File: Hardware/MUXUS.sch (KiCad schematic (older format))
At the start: 3 parts

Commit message: Checkpoint
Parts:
- added C? (x18): 100nF, symbol Device:C_Small
- added C?: 4.7uF, symbol Device:C_Small
- added R?: 12K, symbol Device:R
- added R? (x3): 4K7, symbol Device:R
- added R? (x4): 200K, symbol Device:R
- added R?: 56K, symbol Device:R
- added U?: USB7002_KDX, QFN40P1200X1200X90-101N, symbol USB7002_KDX:USB7002_KDX
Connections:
- net +3V3: now reaches U?.2 (VDD/VDDA)
- net +3V3: now also C?.1, C?.1, C?.2, C?.2, C?.2, C?.2, C?.2, C?.2, C?.2, C?.2, R?.2, U?.26 (VDD33), U?.44 (VDD33), U?.53 (VDD33), U?.62 (VDD33), U?.67 (VDD33), U?.79 (VDD33), U?.86 (VDD33), U?.99 (VDD33)
- net GND: now reaches U?.3 (VSS/VSSA)
- net GND: now also C?.1, C?.1, C?.1, C?.1, C?.1, C?.1, C?.1, C?.1, C?.2, C?.2, C?.2, C?.2, C?.2, C?.2, C?.2, C?.2, C?.2, C?.2, C?.2, R?.1, R?.1, R?.1, R?.1, R?.1, R?.2, R?.2, U?.101 (VSS), U?.24 (TESTEN), U?.96 (ATEST)
- net NRST: now reaches U?.4 (PA0/PA1/PA2/NRST)
- net NRST: now also U?.1 (RESET_N)
- net SLV_I2C_CLK: now reaches U?.5 (PA8/PA11[PA9]/PB0/PB1)
- net SLV_I2C_CLK: now also U?.75 (PF26)
- net SLV_I2C_DATA: now reaches U?.6 (PA12[PA10])
- net SLV_I2C_DATA: now also U?.76 (PF27)
- net SYS_SWDIO: now reaches U?.7 (PA13)
- net SYS_SWCLK: now reaches U?.8 (PB5/PB6/PA14-BOOT0/PA15)
- new net: R?.2, U?.100 (RBIAS)
- new net: R?.2, U?.21 (CFG_STRAP1)
- new net: R?.2, U?.22 (CFG_STRAP2)
- new net: R?.1, U?.63 (TEST1)
- new net: R?.1, U?.64 (TEST2)
- new net: R?.1, U?.65 (TEST3)
- new net: R?.2, U?.69 (PF20/CFG_NON_REM)
- new net: R?.2, U?.70 (PF22/CFG_BC_EN)
- new net: R?.1, U?.87 (CC1_UP)
- new net +1V2: C?.1, C?.1, C?.1, C?.1, C?.1, C?.1, C?.1, C?.1, C?.1, U?.18 (VDD12), U?.25 (VDD12), U?.33 (VDD12), U?.41 (VDD12), U?.55 (VDD12), U?.78 (VDD12), U?.83 (VDD12), U?.9 (VDD12), U?.93 (VDD12)
- new net MSTR_I2C_CLK: U?.61 (PF18)
- new net MSTR_I2C_DATA: U?.66 (PF19)
- new net VBUS: R?.2
- no-connect marks 0 -> 7
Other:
- note added: "100nF SMD_0603 or smaller"
- moved on the sheet: U?

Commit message: Checkpoint
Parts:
- removed C? (x18): 100nF, symbol Device:C_Small
- removed C?: 4.7uF, symbol Device:C_Small
- removed R?: 12K, symbol Device:R
- removed R? (x3): 4K7, symbol Device:R
- removed R? (x4): 200K, symbol Device:R
- removed R?: 56K, symbol Device:R
- removed U? (x2): HD3SS3202IRSVT, QFN40P180X260X55-16N_HD3SS3202IRSVT, symbol HD3SS3202IRSVT:HD3SS3202IRSVT
- removed U?: STM32G030J6M6, SOIC127P600X175-8N, symbol STM32G030J6M6:STM32G030J6M6
- removed U?: USB7002_KDX, QFN40P1200X1200X90-101N, symbol USB7002_KDX:USB7002_KDX
- added C? (x11): 100nF, Capacitor_SMD:C_0805_2012Metric, symbol Device:C_Small
- added C? (x5): 4.7uF, symbol Device:C_Small
- added C?: 87pF, symbol Device:C
- added C? (x14): 100nF, Capacitor_SMD:C_0805_2012Metric, symbol Device:C
- added C?: 1uF, symbol Device:C_Small
- added C? (x2): 22uF, symbol Device:C
- added C?: 1uF, symbol Device:C
- added C? (x2): 14pF, symbol Device:C
- added C? (x3): 120uF, Capacitor_SMD:C_0805_2012Metric, symbol Device:C
- added D? (x4): AMBER, LED_SMD:LED_1206_3216Metric, symbol Device:LED
- added D? (x4): GREEN, LED_SMD:LED_1206_3216Metric, symbol Device:LED
- added D?: B540C-13-F, Diode_SMD:D_SMC, symbol Device:D_Schottky
- added D? (x4): LED, symbol Device:LED
- added F?: 500mA, Fuse:Fuse_1206_3216Metric, symbol Device:Polyfuse
- added J? (x3): USB_B, 67068-9000:67068-9000, symbol Connector:USB_B
- added J? (x3): USB_A, 67643-0910:67643-0910, symbol Connector:USB_A
- added J?: USB_C_Receptacle_USB2.0, DX07S016JA1R1500:DX07S016JA1R1500, symbol Connector:USB_C_Receptacle_USB2.0
- added J?: STDC14, symbol Connector_Generic:Conn_02x07_Odd_Even
- added L?: SRP6530A-6R8M, SRP6530A-6R8M:SRP6530A-6R8M, symbol Device:L
- added R? (x4): 10K, Resistor_SMD:R_1206_3216Metric, symbol Device:R
- added R?: 15.1K, symbol Device:R
- added R? (x7): 330R, symbol Device:R
- added R?: 31.6K, symbol Device:R_Small
- added R?: 10K, Resistor_SMD:R_1206_3216Metric, symbol Device:R_Small
- added R? (x3): 1K, symbol Device:R
- added R? (x12): 100R, symbol Device:R
- added R?: 12K, symbol Device:R
- added SW?: USER, symbol Switch:SW_Push
- added SW?: RESET, symbol Switch:SW_Push
- added U?: STM32G431K8T6, STM32G431K8T6:STM32G431K8T6, symbol STM32G431K8T6:STM32G431K8T6
- added U?: AOZ1212AI, Package_SO:SO-8_3.9x4.9mm_P1.27mm, symbol AOZ1212AI:AOZ1212AI
- added U?: TS3USBCA420RSVR, symbol TS3USBCA420RSVR:TS3USBCA420RSVR
- added U? (x6): USBLC6-2SC6, Package_TO_SOT_SMD:SOT-23-6, symbol Power_Protection:USBLC6-2SC6
- added U? (x3): AP2151W, Package_TO_SOT_SMD:SOT-23-5, symbol AP2151W:AP2151W
- added U?: USB2504A-JT, Package_QFP:LQFP-64_10x10mm_P0.5mm, symbol USB2504A-JT:USB2504A-JT
- added U?: USBLC6-4SC6, Package_TO_SOT_SMD:SOT-23-6, symbol Power_Protection:USBLC6-4SC6
- added Y?: ATS240C, symbol Device:Crystal
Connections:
- net +3V3: now also C?.1, C?.1, C?.1, C?.1, C?.1, C?.1, C?.2, C?.2, C?.2, C?.2, C?.2, C?.2, J?.3 (Pin_3), L?.2, R?.1, R?.1, R?.1, R?.1, R?.1, R?.1, R?.1, R?.1, R?.1, R?.2, R?.2, R?.2, R?.2, R?.2, R?.2, R?.2, R?.2, R?.2, R?.2, U?.1 (VCC), U?.1 (VDD), U?.1 (VDDA33), U?.12 (I2C_EN), U?.13 (VDDA33), U?.15 (VDDA/VREF+), U?.17 (VDD), U?.23 (PRTPWR_POL), U?.28 (VDD33), U?.51 (SELF_PWR), U?.61 (VDDA33PLL), U?.62 (ATEST/REG_EN), U?.7 (VDDA33)
- net GND: now also C?.1, C?.1, C?.1, C?.1, C?.1, C?.1, C?.1, C?.1, C?.1, C?.1, C?.1, C?.1, C?.1, C?.1, C?.1, C?.1, C?.1, C?.1, C?.1, C?.1, C?.1, C?.1, C?.1, C?.2, C?.2, C?.2, C?.2, C?.2, C?.2, C?.2, C?.2, C?.2, C?.2, C?.2, C?.2, C?.2, C?.2, C?.2, C?.2, D?.2 (A), J?.4 (GND), J?.4 (GND), J?.4 (GND), J?.4 (GND), J?.4 (GND), J?.4 (GND), J?.5 (Pin_5), J?.7 (Pin_7), J?.A1 (GND), J?.A12 (GND), J?.B1 (GND), J?.B12 (GND), R?.1, R?.1, R?.1, R?.1, R?.2, R?.2, R?.2, R?.2, R?.2, R?.2, SW?.2, SW?.2, U?.10 (VSS), U?.14 (VSSA), U?.16 (VSS), U?.16 (VSS), U?.2 (GND), U?.2 (GND), U?.2 (GND), U?.2 (GND), U?.2 (GND), U?.2 (GND), U?.2 (GND), U?.2 (GND), U?.2 (GND), U?.2 (GND), U?.29 (VSS), U?.3 (GND), U?.31 (TEST0), U?.32 (VSS), U?.36 (CFG_SEL0), U?.4 (OEn), U?.4 (VSS), U?.41 (VSS), U?.47 (CLKIN_EN), U?.48 (TEST1), U?.50 (CFG_SEL1), U?.53 (VSS), U?.55 (VSS), U?.59 (CFG_SEL2), U?.64 (VSS), U?.9 (GND)
- net NRST: now also C?.2, J?.12 (Pin_12), R?.1, SW?.1, U?.4 (PG10-NRST)
- net VBUS: now also C?.2, C?.2, C?.2, U?.5 (IN), U?.5 (IN), U?.5 (IN)
- new net: C?.2, D?.1 (K), L?.1, U?.1 (LX)
- new net: C?.1, U?.2 (BST)
- new net: R?.1, R?.2, U?.4 (FB)
- new net: R?.2, U?.5 (COMP)
- new net: C?.2, F?.1, U?.6 (EN), U?.7 (VIN)
- new net: C?.2, U?.8 (VBIAS)
- new net: C?.2, R?.1
- new net: C?.2, J?.S1 (SHIELD), R?.2
- new net: C?.1, J?.5 (Shield), R?.1 (x3)
- new net: C?.1, C?.1, J?.1 (VBUS), U?.1 (OUT), U?.5 (VBUS) (x3)
- new net: C?.2, J?.5 (Shield), R?.2 (x3)
- new net: C?.1, U?.57 (XTAL2), Y?.1
- new net: C?.2, U?.58 (XTAL1/CLKIN), Y?.2
- new net: D?.1 (K), U?.19 (AM4/LED_EN)
- new net: D?.1 (K), U?.20 (GR4/PRT_DIS1)
- new net: D?.1 (K), U?.21 (AM3)
- new net: D?.1 (K), U?.22 (GR3/PRT_DIS0)
- new net: D?.1 (K), U?.24 (AM2/MTT_EN)
- new net: D?.1 (K), U?.25 (GR2/NON_REM1)
- new net: D?.1 (K), U?.26 (AM1/GANG_EN)
- new net: D?.1 (K), U?.27 (GR1/NON_REM0)
- new net: C?.2, C?.2, C?.2, C?.2, U?.30 (VDD18), U?.42 (VDD18), U?.54 (VDD18), U?.60 (VDDA18PLL)
- new net: R?.1, U?.63 (RBIAS)
- new net: D?.2 (A), R?.1 (x8)
- new net: D?.2 (A), R?.2 (x4)
- new net BOOT0: R?.1, U?.31 (PB8-BOOT0)
- new net CC1: J?.A5 (CC1), U?.19 (PA9), U?.29 (PB6), U?.4 (I/O3)
- new net CC2: J?.B5 (CC2), U?.20 (PA10), U?.27 (PB4), U?.6 (I/O4)
- new net DFP1_D+: U?.22 (PA12), U?.6 (USBDP1)
- new net DFP1_D-: U?.21 (PA11), U?.5 (USBDN1)
- new net DFP2_CONN_D+: J?.3 (D+), U?.3 (I/O2)
- new net DFP2_CONN_D-: J?.2 (D-), U?.1 (I/O1)
- new net DFP2_D+: U?.4 (I/O2), U?.8 (USBDP2)
- new net DFP2_D-: U?.6 (I/O1), U?.9 (USBDN2)
- new net DFP2_EN: U?.4 (EN), U?.43 (PRTPWR2)
- new net DFP2_OCSn: U?.3 (~FLG), U?.44 (OCS2_N)
- new net DFP3_CONN_D+: J?.3 (D+), U?.3 (I/O2)
- new net DFP3_CONN_D-: J?.2 (D-), U?.1 (I/O1)
- new net DFP3_D+: U?.12 (USBDP3), U?.4 (I/O2)
- new net DFP3_D-: U?.11 (USBDN3), U?.6 (I/O1)
- new net DFP3_EN: U?.39 (PRTPWR3), U?.4 (EN)
- new net DFP3_OCSn: U?.3 (~FLG), U?.40 (OCS3_N)
- new net DFP4_CONN_D+: J?.3 (D+), U?.3 (I/O2)
- new net DFP4_CONN_D-: J?.2 (D-), U?.1 (I/O1)
- new net DFP4_D+: U?.14 (USBDP4), U?.4 (I/O2)
- new net DFP4_D-: U?.15 (USBDN4), U?.6 (I/O1)
- new net DFP4_EN: U?.37 (PRTPWR4), U?.4 (EN)
- new net DFP4_OCSn: U?.3 (~FLG), U?.38 (OCS4_N)
- new net HUB_RESET: R?.2, U?.13 (PB0), U?.49 (RESET_N)
- new net I2C1_SCL: U?.25 (PA15), U?.35 (SCL/SMBCLK), U?.5 (SEL1/SCL)
- new net I2C1_SDA: R?.2, U?.30 (PB7), U?.34 (SDA/SMBDATA), U?.6 (SEL0/SDA)
- new net I2C1_SMBA: R?.2, U?.28 (PB5)
- new net IFP_D+: U?.11 (SBU1), U?.2 (USBDP0)
- new net IFP_D-: U?.10 (SBU2), U?.3 (USBDN0)
- new net IFP_VBUS: R?.2, U?.12 (PA7), U?.52 (VBUS_DET)
- new net LPUART1_RX: J?.13 (Pin_13), U?.8 (PA3)
- new net LPUART1_TX: J?.14 (Pin_14), U?.7 (PA2)
- new net SWCLK: J?.6 (Pin_6), U?.24 (PA14)
- new net SWDIO: J?.4 (Pin_4), U?.23 (PA13)
- new net SWO: J?.8 (Pin_8), U?.26 (PB3)
- new net UFP1_D+: J?.A6 (D+), J?.B6 (D+), U?.3 (I/O2), U?.7 (LnBp)
- new net UFP1_D-: J?.A7 (D-), J?.B7 (D-), U?.1 (I/O1), U?.8 (LnBn)
- new net UFP1_VBUS: F?.2, J?.A4 (VBUS), J?.A9 (VBUS), J?.B4 (VBUS), J?.B9 (VBUS), U?.5 (VBUS)
- new net UFP2_CONN_D+: J?.3 (D+), U?.1 (I/O1)
- new net UFP2_CONN_D-: J?.2 (D-), U?.3 (I/O2)
- new net UFP2_D+: U?.2 (MIC_GND1/Ln1), U?.6 (I/O1)
- new net UFP2_D-: U?.3 (MIC_GND2/Ln2), U?.4 (I/O2)
- new net UFP2_VBUS: J?.1 (VBUS), U?.5 (VBUS), U?.9 (PA4)
- new net UFP3_CONN_D+: J?.3 (D+), U?.1 (I/O1)
- new net UFP3_CONN_D-: J?.2 (D-), U?.3 (I/O2)
- new net UFP3_D+: U?.14 (LnCp), U?.6 (I/O1)
- new net UFP3_D-: U?.13 (LnCn), U?.4 (I/O2)
- new net UFP3_VBUS: J?.1 (VBUS), U?.10 (PA5), U?.5 (VBUS)
- new net UFP4_CONN_D+: J?.3 (D+), U?.1 (I/O1)
- new net UFP4_CONN_D-: J?.2 (D-), U?.3 (I/O2)
- new net UFP4_D+: U?.16 (LnAp), U?.6 (I/O1)
- new net UFP4_D-: U?.15 (LnAn), U?.4 (I/O2)
- new net UFP4_VBUS: J?.1 (VBUS), U?.11 (PA6), U?.5 (VBUS)
- new net UI_BUTTON: C?.2, R?.1, SW?.1, U?.18 (PA8)
- new net UI_LED1: D?.1 (K), U?.2 (PF0-OSC_IN)
- new net UI_LED2: D?.1 (K), U?.3 (PF1-OSC_OUT)
- new net UI_LED3: D?.1 (K), U?.5 (PA0)
- new net UI_LED4: D?.1 (K), U?.6 (PA1)
- no-connect marks 7 -> 9
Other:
- note added: "create footprint"
- note removed: "100nF SMD_0603 or smaller"

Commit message: Checkpoint
Supposed finalization of first prototype
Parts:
- removed R?: 10K, Resistor_SMD:R_1206_3216Metric, symbol Device:R
- added R12, R13, R14: 10K, Resistor_SMD:R_1206_3216Metric, symbol Device:R
- added R16, R18, R20: 1K, Resistor_SMD:R_1206_3216Metric, symbol Device:R
- C1, C2: renamed from C?; value 14pF -> 15pF; footprint (none) -> Capacitor_SMD:C_0805_2012Metric
- C15, C28, C37: renamed from C?; footprint Capacitor_SMD:C_0805_2012Metric -> Capacitor_THT:C_Radial_D6.3mm_H11.0mm_P2.50mm
- C16, C31: renamed from C?; footprint (none) -> Capacitor_SMD:C_0805_2012Metric
- C25, C4, C5, C6, C7: renamed from C?; footprint (none) -> Capacitor_SMD:C_1206_3216Metric
- C30, C39: renamed from C?; footprint (none) -> Capacitor_SMD:C_1210_3225Metric
- C33: renamed from C?; value 87pF -> 100pF; footprint (none) -> Capacitor_SMD:C_0805_2012Metric
- D10, D11, D12, D9: renamed from D?; footprint (none) -> LED_THT:LED_D5.0mm
- J6: renamed from J?; footprint (none) -> FTSH-107-01-L-DV-K-A:FTSH-107-01-L-DV-K-A
- R1, R10, R11, R15, R17, R19, R24, R25, R28, R29, R30, R31, R33, R34, R5, R6, R7, R8, R9: renamed from R?; footprint (none) -> Resistor_SMD:R_0805_2012Metric
- R2, R21, R23, R35, R4: renamed from R?; footprint (none) -> Resistor_SMD:R_1206_3216Metric
- R32: renamed from R?; value 15.1K -> 15K; footprint (none) -> Resistor_SMD:R_1206_3216Metric
- SW1, SW2: renamed from SW?; footprint (none) -> Button_Switch_SMD:SW_Push_1P1T_NO_6x6mm_H9.5mm
- U6: renamed from U?; footprint (none) -> TS3USBCA420RSVR:TS3USBCA420RSVR
- Y1: renamed from Y?; footprint (none) -> ATS240C:ATS240C
- gave numbers to parts that had none: 60
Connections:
- net UFP1_VBUS is gone; now on net VBUS: F1.2, J1.A4 (VBUS), J1.A9 (VBUS), J1.B4 (VBUS), J1.B9 (VBUS), U1.5 (VBUS)
- net +3V3: now also C26.1, SW1.2
- net BOOT0: now also C26.2, R22.2, SW1.1; no longer R22.1
- net GND: now also R22.1, R16.2, R18.2, R20.2; no longer C26.1, R22.2, SW1.2
- net I2C1_SCL: now also R21.2
- net I2C1_SMBA: no longer R21.2
- net UFP2_VBUS: now also R12.2; no longer U7.9 (PA4)
- net UFP3_VBUS: now also R13.2; no longer U7.10 (PA5)
- net UFP4_VBUS: now also R14.2; no longer U7.11 (PA6)
- removed net UI_BUTTON: C26.2, SW1.1, U7.18 (PA8)
- new net: R13.1, R18.1, U7.10 (PA5)
- new net: R14.1, R16.1, U7.11 (PA6)
- new net: R12.1, R20.1, U7.9 (PA4)
- no-connect marks 9 -> 10
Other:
- moved on the sheet: C26, C27, R21, R22, R23, R27, SW1, SW2

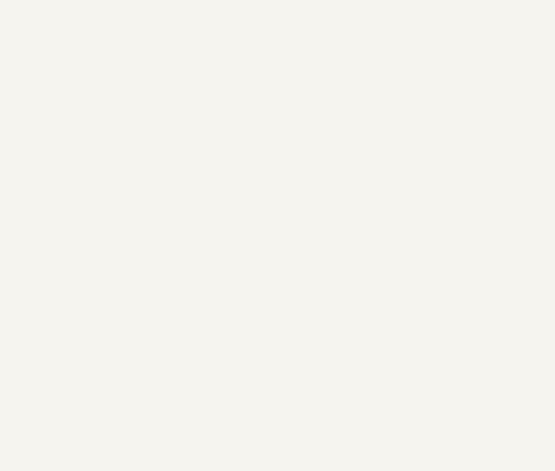
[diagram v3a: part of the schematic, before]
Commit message: Mounting holes
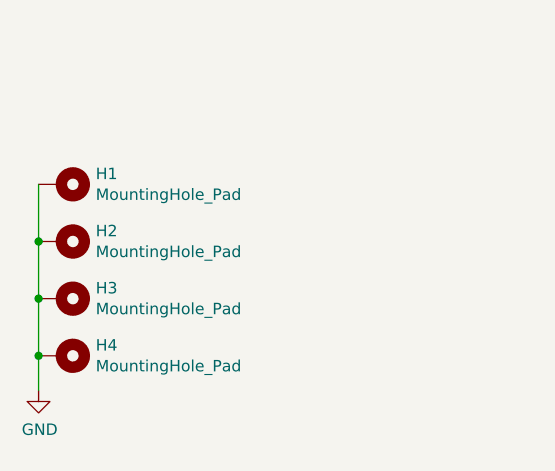
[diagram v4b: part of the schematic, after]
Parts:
- added H1, H2, H3, H4: MountingHole_Pad, MountingHole:MountingHole_3.2mm_M3_Pad_Via, symbol Mechanical:MountingHole_Pad
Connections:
- net GND: now also H1.1, H2.1, H3.1, H4.1
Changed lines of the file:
@@
 Wire Wire Line
 	9500 6700 9850 6700
+$Comp
+L Mechanical:MountingHole_Pad H1
+U 1 1 6152FF69
+P 950 10000
+F 0 "H1" V 904 10150 50  0000 L CNN
+F 1 "MountingHole_Pad" V 995 10150 50  0000 L CNN
+F 2 "MountingHole:MountingHole_3.2mm_M3_Pad_Via" H 950 10000 50  0001 C CNN
+F 3 "~" H 950 10000 50  0001 C CNN
+	1    950  10000
+	0    1    1    0
+$EndComp
+$Comp
+L Mechanical:MountingHole_Pad H3
+U 1 1 615352EC
+P 950 10500
+F 0 "H3" V 904 10650 50  0000 L CNN
+F 1 "MountingHole_Pad" V 995 10650 50  0000 L CNN
+F 2 "MountingHole:MountingHole_3.2mm_M3_Pad_Via" H 950 10500 50  0001 C CNN
+F 3 "~" H 950 10500 50  0001 C CNN
+	1    950  10500
+	0    1    1    0
+$EndComp
+$Comp
+L Mechanical:MountingHole_Pad H2
+U 1 1 61536034
+P 950 10250
+F 0 "H2" V 904 10400 50  0000 L CNN
+F 1 "MountingHole_Pad" V 995 10400 50  0000 L CNN
+F 2 "MountingHole:MountingHole_3.2mm_M3_Pad_Via" H 950 10250 50  0001 C CNN
+F 3 "~" H 950 10250 50  0001 C CNN
+	1    950  10250
+	0    1    1    0
+$EndComp
+$Comp
+L Mechanical:MountingHole_Pad H4
+U 1 1 61536512
+P 950 10750
+F 0 "H4" V 904 10900 50  0000 L CNN
+F 1 "MountingHole_Pad" V 995 10900 50  0000 L CNN
+F 2 "MountingHole:MountingHole_3.2mm_M3_Pad_Via" H 950 10750 50  0001 C CNN
+F 3 "~" H 950 10750 50  0001 C CNN
+	1    950  10750
+	0    1    1    0
+$EndComp
+Wire Wire Line
+	850  10000 850  10250
+Connection ~ 850  10250
+Wire Wire Line
+	850  10250 850  10500
+Connection ~ 850  10500
+Wire Wire Line
+	850  10500 850  10750
+Wire Wire Line
+	850  10750 850  10900
+Connection ~ 850  10750
+$Comp
+L power:GND #PWR037
+U 1 1 615A8863
+P 850 10900
+F 0 "#PWR037" H 850 10650 50  0001 C CNN
+F 1 "GND" H 855 10727 50  0000 C CNN
+F 2 "" H 850 10900 50  0001 C CNN
+F 3 "" H 850 10900 50  0001 C CNN
+	1    850  10900
+	1    0    0    -1
+$EndComp
 $EndSCHEMATC
